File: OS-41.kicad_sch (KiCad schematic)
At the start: 78 parts, among them J1 Conn_01x02_Pin, J2 Conn_01x02_Pin, J3 Conn_01x02_Pin, J4 Conn_Coaxial, J5 Conn_01x02_Pin, J6 USB_B_Micro, J7 Conn_01x09_Pin, SW1 TS-1187A-B-A-B, SW2 TS-1187A-B-A-B, U1 GPS1003, U10 W25Q128JVS, U2 SI4432-B1-FMR, U3 MCP1640x-xCHY, U4 ATGM336H-5N31, U5 DS18B20, U6 BMP390L, U7 RP2040, U8 ABM8-272-T3_C20625731, U9 AMS1117-3.3, X1 SMD-3225_4P 30.000MHZ 10PF

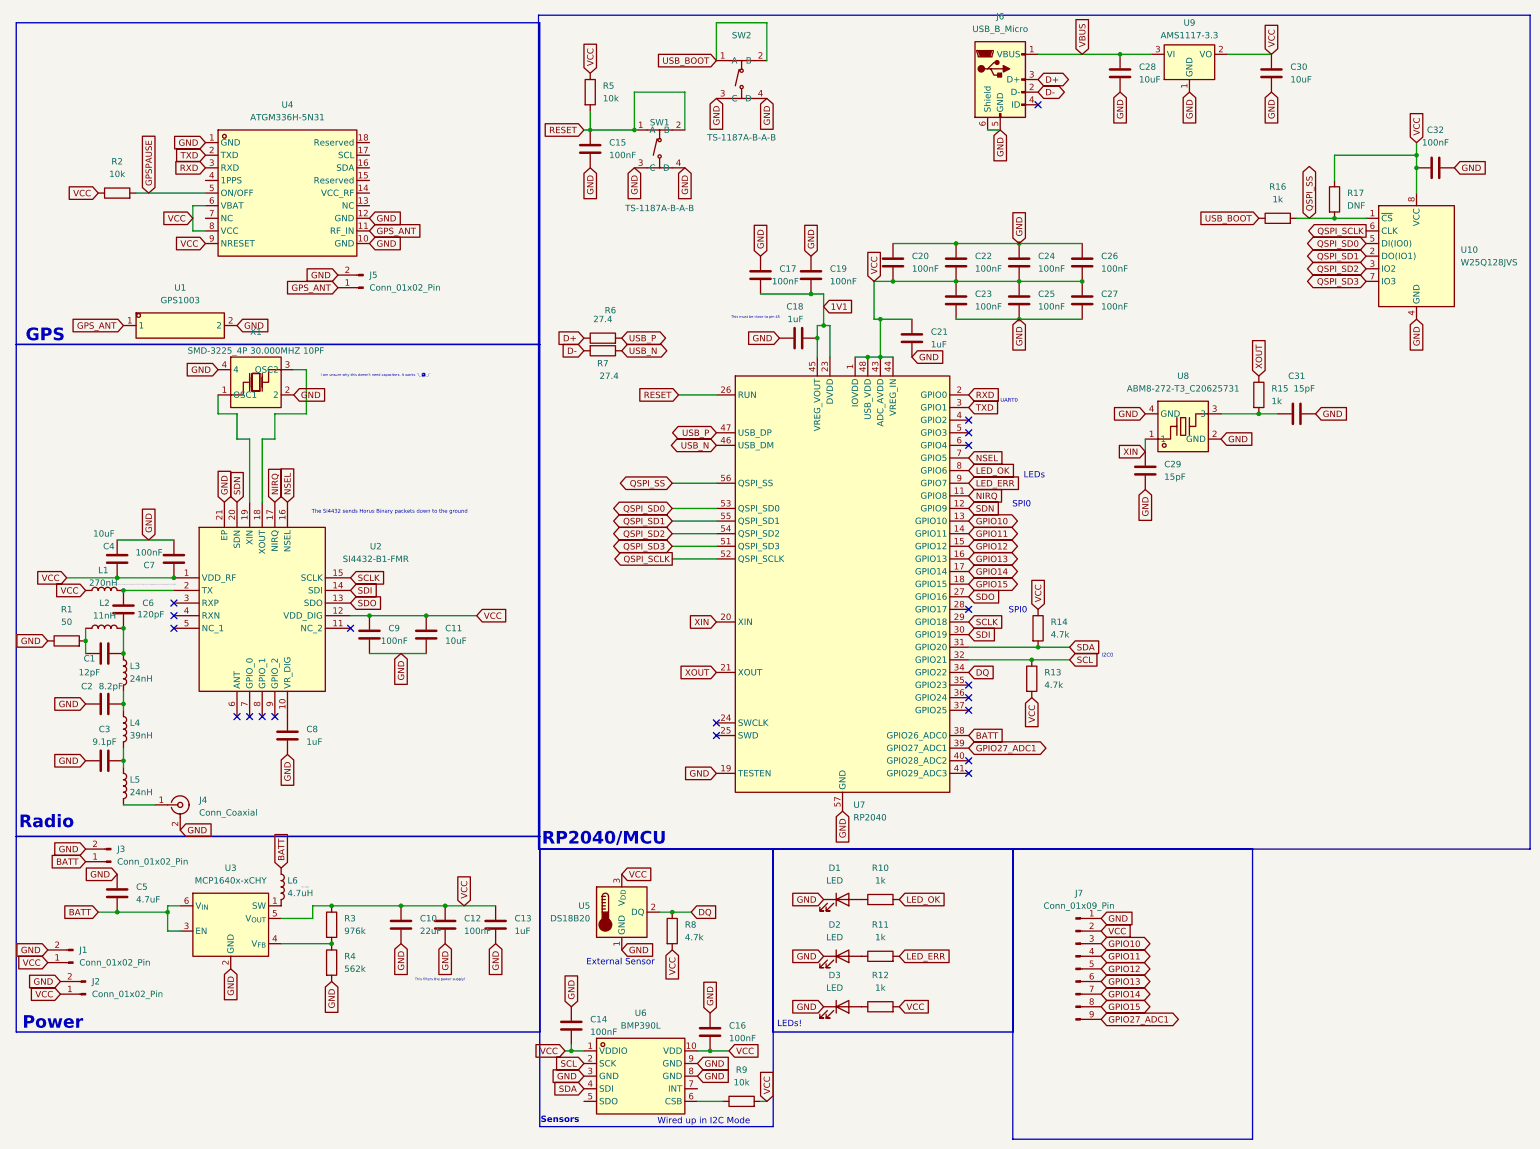
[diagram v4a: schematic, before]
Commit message: Add comments to schematic
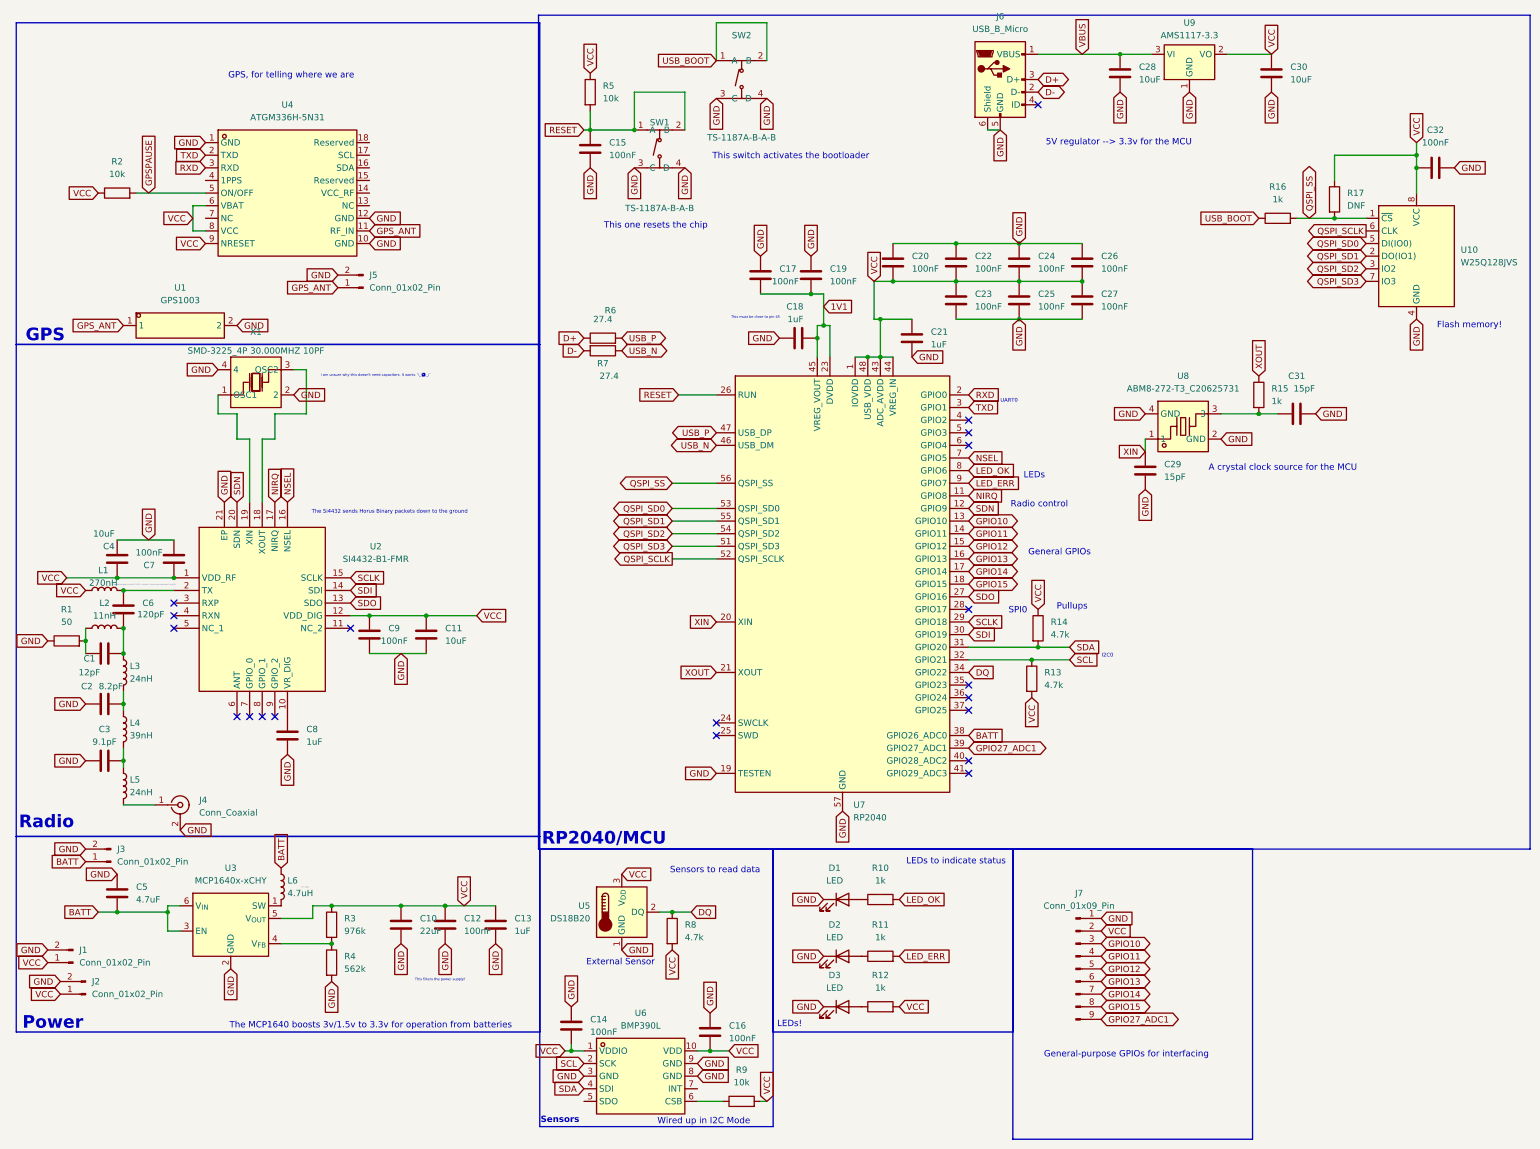
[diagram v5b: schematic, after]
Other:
- note added: "5V regulator --> 3.3v for the MCU"
- note added: "A crystal clock source for the MCU"
- note added: "Flash memory!"
- note added: "GPS, for telling where we are"
- note added: "General GPIOs"
- note added: "General-purpose GPIOs for interfacing"
- note added: "LEDs to indicate status"
- note added: "Pullups"
- note added: "Radio control"
- note added: "Sensors to read data"
- note added: "The MCP1640 boosts 3v/1.5v to 3.3v for operation from batteries"
- note added: "This one resets the chip"
- note added: "This switch activates the bootloader"
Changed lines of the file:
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@@
+		)
+	)
+	(text "General-purpose GPIOs for interfacing"
+		(exclude_from_sim no)
+		(at 237.49 224.282 0)
+		(effects
+			(font
+				(size 1.27 1.27)
+			)
 		)
 	)
@@
 		)
 	)
+	(text "General GPIOs"
+		(exclude_from_sim no)
+		(at 224.028 123.19 0)
+		(effects
+			(font
+				(size 1.27 1.27)
+			)
+		)
+	)
 	(text "External Sensor"
 		(exclude_from_sim no)
@@
 		)
 	)
+	(text "LEDs to indicate status"
+		(exclude_from_sim no)
+		(at 203.2 185.42 0)
+		(effects
+			(font
+				(size 1.27 1.27)
+			)
+		)
+	)
+	(text "Pullups"
+		(exclude_from_sim no)
+		(at 226.568 134.112 0)
+		(effects
+			(font
+				(size 1.27 1.27)
+			)
+		)
+	)
 	(text "UART0"
 		(exclude_from_sim no)
@@
 		)
 	)
+	(text "This switch activates the bootloader"
+		(exclude_from_sim no)
+		(at 169.926 43.434 0)
+		(effects
+			(font
+				(size 1.27 1.27)
+			)
+		)
+	)
 	(text "This must be close to pin 45"
 		(exclude_from_sim no)
@@
 		)
 	)
+	(text "GPS, for telling where we are"
+		(exclude_from_sim no)
+		(at 69.342 27.178 0)
+		(effects
+			(font
+				(size 1.27 1.27)
+			)
+		)
+	)
+	(text "Sensors to read data"
+		(exclude_from_sim no)
+		(at 154.686 187.198 0)
+		(effects
+			(font
+				(size 1.27 1.27)
+			)
+		)
+	)
 	(text "LEDs!"
 		(exclude_from_sim no)
@@
 		)
 	)
-	(text "SPI0"
-		(exclude_from_sim no)
-		(at 216.408 113.538 0)
+	(text "The MCP1640 boosts 3v/1.5v to 3.3v for operation from batteries"
+		(exclude_from_sim no)
+		(at 85.344 218.44 0)
+		(effects
+			(font
+				(size 1.27 1.27)
+			)
+		)
+	)
+	(text "Radio control"
+		(exclude_from_sim no)
+		(at 219.964 113.538 0)
 		(effects
 			(font
@@
 		)
 	)
+	(text "Flash memory!"
+		(exclude_from_sim no)
+		(at 306.578 77.47 0)
+		(effects
+			(font
+				(size 1.27 1.27)
+			)
+		)
+	)
 	(text "Wired up in I2C Mode"
 		(exclude_from_sim no)
@@
 		)
 	)
+	(text "This one resets the chip"
+		(exclude_from_sim no)
+		(at 142.748 57.404 0)
+		(effects
+			(font
+				(size 1.27 1.27)
+			)
+		)
+	)
 	(text "GPS"
 		(exclude_from_sim no)
@@
 		)
 	)
+	(text "A crystal clock source for the MCU"
+		(exclude_from_sim no)
+		(at 268.986 106.172 0)
+		(effects
+			(font
+				(size 1.27 1.27)
+			)
+		)
+	)
 	(text "Note: I initially really messed the matching up. The Si4432 PA is a switching PA, so it needs some unusual matching networks. Check out AN435"
 		(exclude_from_sim no)
@@
 			)
 		)
+	)
+	(text "5V regulator --> 3.3v for the MCU"
+		(exclude_from_sim no)
+		(at 235.966 40.64 0)
+		(effects
+			(font
+				(size 1.27 1.27)
+			)
+		)

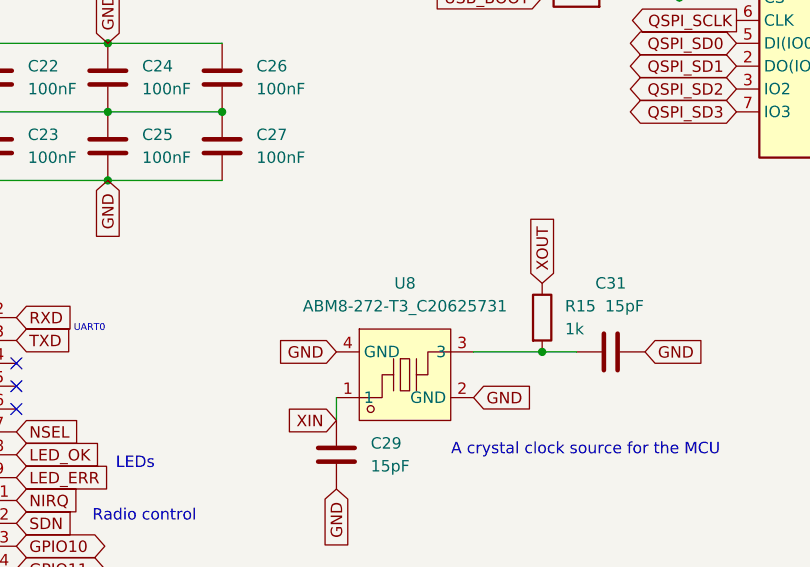
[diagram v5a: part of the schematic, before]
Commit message: Change designator to X2
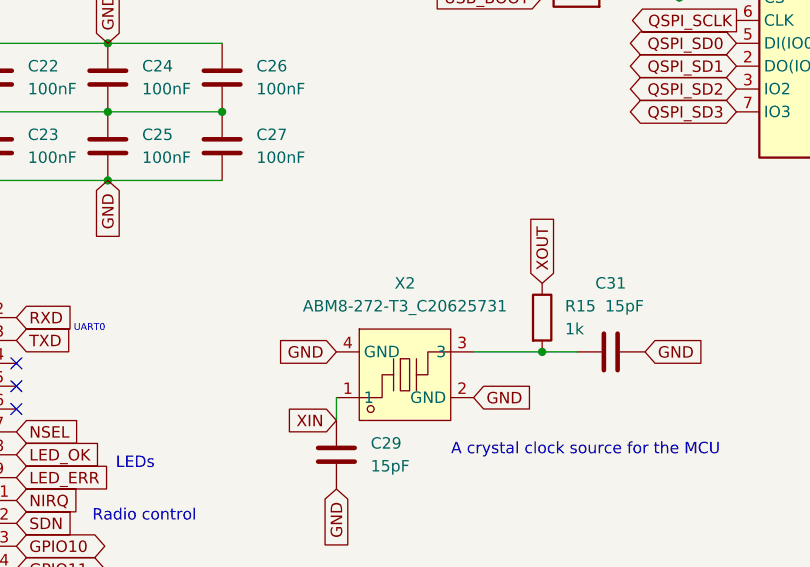
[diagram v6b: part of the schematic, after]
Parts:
- renumbered U8 to X2
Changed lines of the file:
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@@
 		(dnp no)
 		(fields_autoplaced yes)
-		(property "Reference" "U8"
+		(property "Reference" "X2"
 			(at 248.92 87.63 0)
 			(effects
@@
 			(project ""
 				(path "/d2225c9f-058e-4f40-b93c-9ee01fd58030"
-					(reference "U8")
+					(reference "X2")
 					(unit 1)
 				)

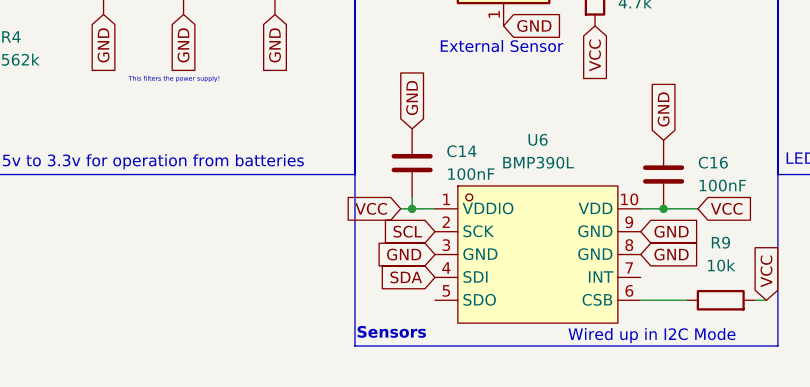
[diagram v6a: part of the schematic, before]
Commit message: BMP390 oops (add pullup resistor for address selection)
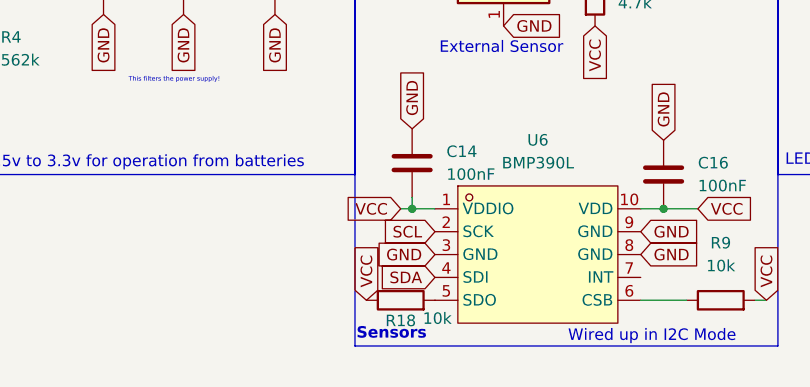
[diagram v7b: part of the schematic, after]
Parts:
- added R18: 10k, Resistor_SMD:R_0603_1608Metric_Pad0.98x0.95mm_HandSolder, symbol Device:R
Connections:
- net VCC: now also R18.1
- net at U6.5 (SDO): now also R18.2
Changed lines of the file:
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@@
 		)
 	)
+	(global_label "VCC"
+		(shape input)
+		(at 120.65 233.68 90)
+		(fields_autoplaced yes)
+		(effects
+			(font
+				(size 1.27 1.27)
+			)
+			(justify left)
+		)
+		(property "Intersheetrefs" "${INTERSHEET_REFS}"
+			(at 120.65 227.0662 90)
+			(effects
+				(font
+					(size 1.27 1.27)
+				)
+				(justify left)
+				(hide yes)
+			)
+		)
+	)
 	(global_label "SCL"
 		(shape input)
@@
 					(unit 1)
 				)
+			)
+		)
+	)
+	(symbol
+		(lib_id "Device:R")
+		(at 124.46 233.68 90)
+		(unit 1)
+		(exclude_from_sim no)
+		(in_bom yes)
+		(on_board yes)
+		(dnp no)
+		(property "Reference" "R18"
+			(at 124.46 235.966 90)
+			(effects
+				(font
+					(size 1.27 1.27)
+				)
+			)
+		)
+		(property "Value" "10k"
+			(at 128.524 235.712 90)
+			(effects
+				(font
+					(size 1.27 1.27)
+				)
+			)
+		)
+		(property "Footprint" "Resistor_SMD:R_0603_1608Metric_Pad0.98x0.95mm_HandSolder"
+			(at 124.46 235.458 90)
+			(effects
+				(font
+					(size 1.27 1.27)
+				)
+				(hide yes)
+			)
+		)
+		(property "Datasheet" "~"
+			(at 124.46 233.68 0)
+			(effects
+				(font
+					(size 1.27 1.27)
+				)
+				(hide yes)
+			)
+		)
+		(property "Description" "Resistor"
+			(at 124.46 233.68 0)
+			(effects
+				(font
+					(size 1.27 1.27)
+				)
+				(hide yes)
+			)
+		)
+		(pin "1"
+		)
+		(pin "2"
+		)
+		(instances
+			(project "OS-41"
+				(path "/d2225c9f-058e-4f40-b93c-9ee01fd58030"
+					(reference "R18")
+					(unit 1)
+				)

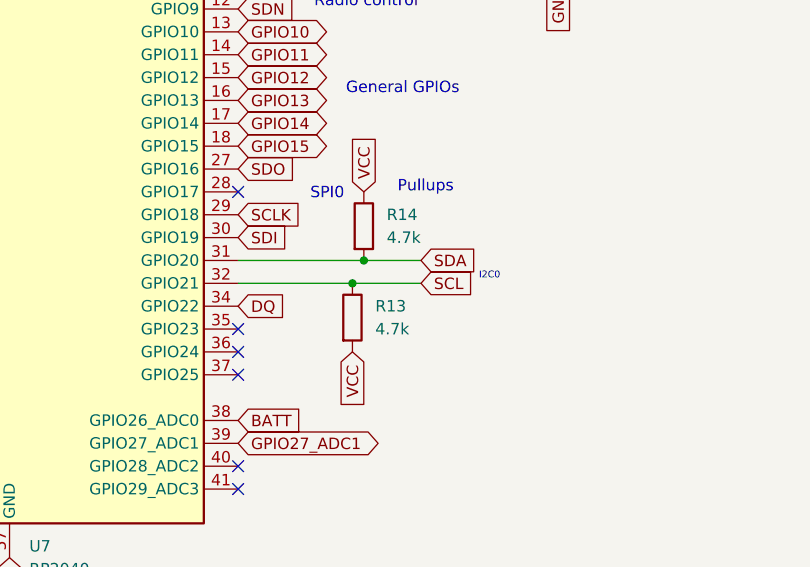
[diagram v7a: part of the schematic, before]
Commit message: Change I2C pullup values
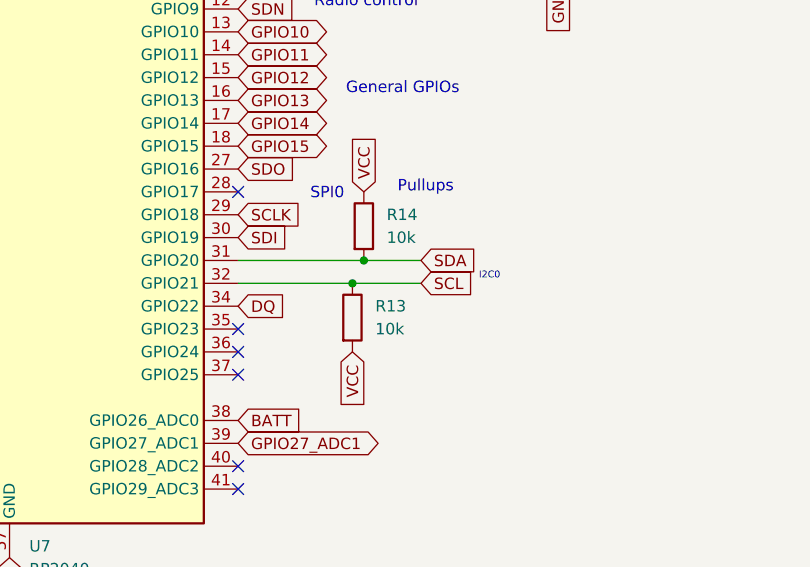
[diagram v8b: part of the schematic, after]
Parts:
- R13, R14: value 4.7k -> 10k
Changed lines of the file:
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@@
 			)
 		)
-		(property "Value" "4.7k"
+		(property "Value" "10k"
 			(at 222.25 139.6999 0)
 			(effects
@@
 			)
 		)
-		(property "Value" "4.7k"
+		(property "Value" "10k"
 			(at 220.98 149.8599 0)
 			(effects
